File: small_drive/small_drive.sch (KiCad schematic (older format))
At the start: 79 parts, among them CON1 BARREL_JACK, J1 DB9, M1 SiR826DP, M2 SiR826DP, M3 SiR826DP, M4 SiR826DP, M5 SiR826DP, M6 SiR826DP, P2 CONN_01X04, P3 CONN_01X06, P4 CONN_01X08, P5 CONN_01X02, P6 CONN_01X02, P7 CONN_01X02, U1 STM32F334K8, U10 LM5106, U11 ACS711ELCTR-25AB-T, U12 ACS711ELCTR-25AB-T, U13 ACS711ELCTR-25AB-T, U2 OKR_T3, U3 LTC2850, U4 LTC2850, U5 LTC2850, U6 LT1764EQ, U7 MC33074DTBR2, U8 LM5106, U9 LM5106

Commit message: Before splitting.
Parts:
- added C? (x2): C, symbol C
- added Y?: Crystal, symbol Crystal
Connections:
- wire segments 350 -> 360
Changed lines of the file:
@@
 Wire Wire Line
 	2750 4300 2750 4400
+$Comp
+L Crystal Y?
+U 1 1 578406AE
+P 2000 4600
+F 0 "Y?" H 2000 4750 50  0000 C CNN
+F 1 "Crystal" H 2000 4450 50  0000 C CNN
+F 2 "" H 2000 4600 50  0000 C CNN
+F 3 "" H 2000 4600 50  0000 C CNN
+	1    2000 4600
+	1    0    0    -1
+$EndComp
+$Comp
+L C C?
+U 1 1 578407A7
+P 1750 4200
+F 0 "C?" H 1800 4300 50  0000 L CNN
+F 1 "C" H 1800 4100 50  0000 L CNN
+F 2 "" H 1750 4200 60  0000 C CNN
+F 3 "" H 1750 4200 60  0000 C CNN
+	1    1750 4200
+	1    0    0    -1
+$EndComp
+$Comp
+L C C?
+U 1 1 5784091C
+P 2250 4200
+F 0 "C?" H 2300 4300 50  0000 L CNN
+F 1 "C" H 2300 4100 50  0000 L CNN
+F 2 "" H 2250 4200 60  0000 C CNN
+F 3 "" H 2250 4200 60  0000 C CNN
+	1    2250 4200
+	1    0    0    -1
+$EndComp
+Wire Wire Line
+	2250 4400 2250 4950
+Wire Wire Line
+	2250 4600 2150 4600
+Wire Wire Line
+	2250 4950 1450 4950
+Connection ~ 2250 4600
+Wire Wire Line
+	1450 4850 1750 4850
+Wire Wire Line
+	1750 4850 1750 4400
+Wire Wire Line
+	1750 4600 1850 4600
+Connection ~ 1750 4600
+$Comp
+L GND #PWR?
+U 1 1 57841258
+P 2000 3900
+F 0 "#PWR?" H 2000 3650 50  0001 C CNN
+F 1 "GND" H 2000 3750 50  0000 C CNN
+F 2 "" H 2000 3900 50  0000 C CNN
+F 3 "" H 2000 3900 50  0000 C CNN
+	1    2000 3900
+	-1   0    0    1
+$EndComp
+Wire Wire Line
+	2250 3950 2250 4000
+Wire Wire Line
+	1750 3950 2250 3950
+Wire Wire Line
+	1750 3950 1750 4000
+Wire Wire Line
+	2000 3950 2000 3900
+Connection ~ 2000 3950
 $EndSCHEMATC

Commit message: PCB ordered
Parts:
- C48, C49: renamed from C?; footprint (none) -> Capacitors_SMD:C_0603
- Y1: renamed from Y?; footprint (none) -> Crystals:QC3CA

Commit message: Adding order codes
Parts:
- C1, C14, C2, C4, C5, C6: symbol CP -> CP-RESCUE-small_drive
- CON1: Farnell (none) -> 1243245
- P3: Farnell (none) -> 1125375; Manufacturer (none) -> MOLEX; PartNr (none) -> 53261-0671
- P4: Farnell (none) -> 1125376; Manufacturer (none) -> MOLEX; PartNr (none) -> 53261-0871
- U11, U13: value ACS711ELCTR-25AB-T -> ACS711KLCTR-12AB-T; Farnell (none) -> 2057423
- U12: Farnell (none) -> 2057423; PartNr ACS711ELCTR-25AB-T -> ACS711KLCTR-12AB-T
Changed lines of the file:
@@
 $Descr A3 16535 11693
 encoding utf-8
-Sheet 1 4
+Sheet 1 1
 Title ""
 Date ""
@@
 P 14000 3600
 F 0 "U11" H 14000 3900 60  0000 C CNN
-F 1 "ACS711ELCTR-25AB-T" H 14000 3300 60  0000 C CNN
+F 1 "ACS711KLCTR-12AB-T" H 14000 3300 60  0000 C CNN
 F 2 "Housings_SOIC:SOIC-8_3.9x4.9mm_Pitch1.27mm" H 13900 3850 60  0001 C CNN
 F 3 "" H 14000 3600 60  0000 C CNN
-F 4 "620-1371-1-ND" H 14200 4150 60  0001 C CNN "Digikey"
-F 5 "ACS711ELCTR-25AB-T" H 14400 4350 60  0001 C CNN "PartNr"
+F 4 "2057423" H 14000 3600 60  0001 C CNN "Farnell"
+F 5 "620-1371-1-ND" H 14200 4150 60  0001 C CNN "Digikey"
 F 6 "Allegro" H 14300 4250 60  0001 C CNN "Manufacturer"
+F 7 "ACS711ELCTR-25AB-T" H 14400 4350 60  0001 C CNN "PartNr"
 	1    14000 3600
 	1    0    0    -1
@@
 $EndComp
 $Comp
-L GND #PWR02
+L GND-RESCUE-small_drive #PWR02
 U 1 1 5761D72D
 P 10700 2450
@@
 $EndComp
 $Comp
-L GND #PWR04
+L GND-RESCUE-small_drive #PWR04
 U 1 1 5763B708
 P 9800 5050
@@
 F 2 "Housings_SOIC:SOIC-8_3.9x4.9mm_Pitch1.27mm" H 13900 6350 60  0001 C CNN
 F 3 "" H 14000 6100 60  0000 C CNN
-F 4 "620-1371-1-ND" H 14200 6650 60  0001 C CNN "Digikey"
-F 5 "ACS711ELCTR-25AB-T" H 14400 6850 60  0001 C CNN "PartNr"
+F 4 "2057423" H 14000 6100 60  0001 C CNN "Farnell"
+F 5 "620-1371-1-ND" H 14200 6650 60  0001 C CNN "Digikey"
 F 6 "Allegro" H 14300 6750 60  0001 C CNN "Manufacturer"
+F 7 "ACS711KLCTR-12AB-T" H 14400 6850 60  0001 C CNN "PartNr"
 	1    14000 6100
 	1    0    0    -1
@@
 $EndComp
 $Comp
-L GND #PWR07
+L GND-RESCUE-small_drive #PWR07
 U 1 1 576581B1
 P 10700 4950
@@
 $EndComp
 $Comp
-L GND #PWR09
+L GND-RESCUE-small_drive #PWR09
 U 1 1 576581ED
 P 9800 7550
@@
 $EndComp
 $Comp
-L GND #PWR012
+L GND-RESCUE-small_drive #PWR012
 U 1 1 57658859
 P 10700 7450
@@
 $EndComp
 $Comp
-L GND #PWR014
+L GND-RESCUE-small_drive #PWR014
 U 1 1 57658895
 P 9800 10050
@@
 $EndComp
 $Comp
-L GND #PWR016
+L GND-RESCUE-small_drive #PWR016
 U 1 1 57659CCA
 P 12200 4200
@@
 $EndComp
 $Comp
-L GND #PWR017
+L GND-RESCUE-small_drive #PWR017
 U 1 1 57659FBD
 P 12200 6700
@@
 $EndComp
 $Comp
-L GND #PWR018
+L GND-RESCUE-small_drive #PWR018
 U 1 1 5765A1D2
 P 12200 9200
@@
 $EndComp
 $Comp
-L GND #PWR022
+L GND-RESCUE-small_drive #PWR022
 U 1 1 5779740F
 P 4700 9650
@@
 $EndComp
 $Comp
-L GND #PWR023
+L GND-RESCUE-small_drive #PWR023
 U 1 1 577976BF
 P 1550 6750
@@
 $EndComp
 $Comp
-L GND #PWR024
+L GND-RESCUE-small_drive #PWR024
 U 1 1 577978BD
 P 1550 9200
@@
 $EndComp
 $Comp
-L GND #PWR028
+L GND-RESCUE-small_drive #PWR028
 U 1 1 57798BD2
 P 3450 5650
@@
 $EndComp
 $Comp
-L GND #PWR029
+L GND-RESCUE-small_drive #PWR029
 U 1 1 5779A5C8
 P 6950 10000
@@
 $EndComp
 $Comp
-L GND #PWR031
+L GND-RESCUE-small_drive #PWR031
 U 1 1 5779B645
 P 2450 8100
@@
 $EndComp
 $Comp
-L GND #PWR033
+L GND-RESCUE-small_drive #PWR033
 U 1 1 5779C4DD
 P 5700 8600
@@
 $EndComp
 $Comp
-L CP C2
+L CP-RESCUE-small_drive C2
 U 1 1 577CA002
 P 1750 3150
@@
 $EndComp
 $Comp
-L CP C4
+L CP-RESCUE-small_drive C4
 U 1 1 577CA310
 P 2300 3150
@@
 $EndComp
 $Comp
-L CP C5
+L CP-RESCUE-small_drive C5
 U 1 1 577CA388
 P 2850 3150
@@
 $EndComp
 $Comp
-L GND #PWR037
+L GND-RESCUE-small_drive #PWR037
 U 1 1 577CA455
 P 2000 3400
@@
 F 2 "00_Passives:smd_barrel_jack" H 1150 1050 60  0001 C CNN
 F 3 "" H 1150 1050 60  0000 C CNN
+F 4 "1243245" H 1150 1050 60  0001 C CNN "Farnell"
 	1    1150 1050
 	1    0    0    -1
@@
 $EndComp
 $Comp
-L CP C1
+L CP-RESCUE-small_drive C1
 U 1 1 577CE3D8
 P 1700 1250
@@
 $EndComp
 $Comp
-L CP C6
+L CP-RESCUE-small_drive C6
 U 1 1 577CF084
 P 4000 1250
@@
 $EndComp
 $Comp
-L GND #PWR041
+L GND-RESCUE-small_drive #PWR041
 U 1 1 577D3636
 P 4750 2250
@@
 $EndComp
 $Comp
-L CP C14
+L CP-RESCUE-small_drive C14
 U 1 1 577D4059
 P 8350 1250
@@
 F 2 "Connectors_Molex:Molex_PicoBlade_53261-0871" H 7350 9500 50  0001 C CNN
 F 3 "" H 7350 9500 50  0000 C CNN
+F 4 "1125376" H 7350 9500 60  0001 C CNN "Farnell"
+F 5 "MOLEX" H 7350 9500 60  0001 C CNN "Manufacturer"
+F 6 "53261-0871" H 7350 9500 60  0001 C CNN "PartNr"
 	1    7350 9500
 	1    0    0    -1
@@
 F 2 "Connectors_Molex:Molex_PicoBlade_53261-0671" H 6100 8200 50  0001 C CNN
 F 3 "" H 6100 8200 50  0000 C CNN
+F 4 "1125375" H 6100 8200 60  0001 C CNN "Farnell"
+F 5 "MOLEX" H 6100 8200 60  0001 C CNN "Manufacturer"
+F 6 "53261-0671" H 6100 8200 60  0001 C CNN "PartNr"
 	1    6100 8200
 	1    0    0    -1
@@
 P 14000 8600
 F 0 "U13" H 14000 8900 60  0000 C CNN
-F 1 "ACS711ELCTR-25AB-T" H 14000 8300 60  0000 C CNN
+F 1 "ACS711KLCTR-12AB-T" H 14000 8300 60  0000 C CNN
 F 2 "Housings_SOIC:SOIC-8_3.9x4.9mm_Pitch1.27mm" H 13900 8850 60  0001 C CNN
 F 3 "" H 14000 8600 60  0000 C CNN
-F 4 "620-1371-1-ND" H 14200 9150 60  0001 C CNN "Digikey"
-F 5 "ACS711ELCTR-25AB-T" H 14400 9350 60  0001 C CNN "PartNr"
+F 4 "2057423" H 14000 8600 60  0001 C CNN "Farnell"
+F 5 "620-1371-1-ND" H 14200 9150 60  0001 C CNN "Digikey"
 F 6 "Allegro" H 14300 9250 60  0001 C CNN "Manufacturer"
+F 7 "ACS711ELCTR-25AB-T" H 14400 9350 60  0001 C CNN "PartNr"
 	1    14000 8600
 	1    0    0    -1
@@
 $EndComp
 $Comp
-L GND #PWR043
+L GND-RESCUE-small_drive #PWR043
 U 1 1 57818AED
 P 15300 6200
@@
 $EndComp
 $Comp
-L GND #PWR045
+L GND-RESCUE-small_drive #PWR045
 U 1 1 57819A33
 P 15300 8700
@@
 $EndComp
 $Comp
-L GND #PWR047
+L GND-RESCUE-small_drive #PWR047
 U 1 1 57838A84
 P 7650 6150
@@
 	7650 5100 7650 5200
 $Comp
-L GND #PWR049
+L GND-RESCUE-small_drive #PWR049
 U 1 1 5783BEEB
 P 2450 5600
@@
 Connection ~ 2250 4600
 Wire Wire Line
-	1450 4850 1750 4850
-Wire Wire Line
-	1750 4850 1750 4400
+	1750 4850 1450 4850
+Wire Wire Line
+	1750 4400 1750 4850
 Wire Wire Line
 	1750 4600 1850 4600
 Connection ~ 1750 4600
 $Comp
-L GND #PWR051
+L GND-RESCUE-small_drive #PWR051
 U 1 1 57841258
 P 2000 3900

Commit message: Encoder TXD matched with mitsubishi drive.
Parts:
- U10, U8, U9: symbol LM5106-RESCUE-small_drive -> LM5106-RESCUE-small_drive-RESCUE-small_drive
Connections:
- wire segments 360 -> 362
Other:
- moved on the sheet: C14, C15, C16, C17, C18, C8, U6
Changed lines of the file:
@@
 $EndComp
 $Comp
-L LM5106-RESCUE-small_drive U8
+L LM5106-RESCUE-small_drive-RESCUE-small_drive U8
 U 1 1 5761CB0B
 P 11450 3300
@@
 $EndComp
 $Comp
-L LM5106-RESCUE-small_drive U9
+L LM5106-RESCUE-small_drive-RESCUE-small_drive U9
 U 1 1 576581B9
 P 11450 5800
@@
 $EndComp
 $Comp
-L LM5106-RESCUE-small_drive U10
+L LM5106-RESCUE-small_drive-RESCUE-small_drive U10
 U 1 1 57658861
 P 11450 8300
@@
 L LT1764EQ U6
 U 1 1 577CDD60
-P 7500 1100
-F 0 "U6" H 7350 700 60  0000 C CNN
-F 1 "LT1764EQ" H 7500 1400 60  0000 C CNN
-F 2 "00_Passives:DD-PAK" H 7550 1100 60  0001 C CNN
-F 3 "" H 7500 1100 60  0000 C CNN
-F 4 "46" H 7500 1525 60  0001 C CNN "Voorraad"
-	1    7500 1100
+P 7600 1100
+F 0 "U6" H 7450 700 60  0000 C CNN
+F 1 "LT1764EQ" H 7600 1400 60  0000 C CNN
+F 2 "00_Passives:DD-PAK" H 7650 1100 60  0001 C CNN
+F 3 "" H 7600 1100 60  0000 C CNN
+F 4 "46" H 7600 1525 60  0001 C CNN "Voorraad"
+	1    7600 1100
 	1    0    0    -1
 $EndComp
@@
 L C C15
 U 1 1 577D4053
-P 8900 1250
-F 0 "C15" H 8950 1350 50  0000 L CNN
-F 1 "100nF" H 8950 1150 50  0000 L CNN
-F 2 "Capacitors_SMD:C_0603" H 8900 1250 60  0001 C CNN
-F 3 "" H 8900 1250 60  0000 C CNN
-	1    8900 1250
+P 9000 1250
+F 0 "C15" H 9050 1350 50  0000 L CNN
+F 1 "100nF" H 9050 1150 50  0000 L CNN
+F 2 "Capacitors_SMD:C_0603" H 9000 1250 60  0001 C CNN
+F 3 "" H 9000 1250 60  0000 C CNN
+	1    9000 1250
 	1    0    0    -1
 $EndComp
@@
 L CP-RESCUE-small_drive C14
 U 1 1 577D4059
-P 8350 1250
-F 0 "C14" H 8375 1350 50  0000 L CNN
-F 1 "100uF/35V" H 8375 1150 50  0000 L CNN
-F 2 "Capacitors_SMD:c_elec_8x10.5" H 8388 1100 50  0001 C CNN
-F 3 "" H 8350 1250 50  0000 C CNN
-	1    8350 1250
+P 8450 1250
+F 0 "C14" H 8475 1350 50  0000 L CNN
+F 1 "100uF/35V" H 8475 1150 50  0000 L CNN
+F 2 "Capacitors_SMD:c_elec_8x10.5" H 8488 1100 50  0001 C CNN
+F 3 "" H 8450 1250 50  0000 C CNN
+	1    8450 1250
 	1    0    0    -1
 $EndComp
@@
 L C C16
 U 1 1 577D405F
-P 9250 1250
-F 0 "C16" H 9300 1350 50  0000 L CNN
-F 1 "100nF" H 9300 1150 50  0000 L CNN
-F 2 "Capacitors_SMD:C_0603" H 9250 1250 60  0001 C CNN
-F 3 "" H 9250 1250 60  0000 C CNN
-	1    9250 1250
+P 9350 1250
+F 0 "C16" H 9400 1350 50  0000 L CNN
+F 1 "100nF" H 9400 1150 50  0000 L CNN
+F 2 "Capacitors_SMD:C_0603" H 9350 1250 60  0001 C CNN
+F 3 "" H 9350 1250 60  0000 C CNN
+	1    9350 1250
 	1    0    0    -1
 $EndComp
@@
 L C C17
 U 1 1 577D4065
-P 9600 1250
-F 0 "C17" H 9650 1350 50  0000 L CNN
-F 1 "100nF" H 9650 1150 50  0000 L CNN
-F 2 "Capacitors_SMD:C_0603" H 9600 1250 60  0001 C CNN
-F 3 "" H 9600 1250 60  0000 C CNN
-	1    9600 1250
+P 9700 1250
+F 0 "C17" H 9750 1350 50  0000 L CNN
+F 1 "100nF" H 9750 1150 50  0000 L CNN
+F 2 "Capacitors_SMD:C_0603" H 9700 1250 60  0001 C CNN
+F 3 "" H 9700 1250 60  0000 C CNN
+	1    9700 1250
 	1    0    0    -1
 $EndComp
@@
 L C C18
 U 1 1 577D406B
-P 9950 1250
-F 0 "C18" H 10000 1350 50  0000 L CNN
-F 1 "100nF" H 10000 1150 50  0000 L CNN
-F 2 "Capacitors_SMD:C_0603" H 9950 1250 60  0001 C CNN
-F 3 "" H 9950 1250 60  0000 C CNN
-	1    9950 1250
+P 10050 1250
+F 0 "C18" H 10100 1350 50  0000 L CNN
+F 1 "100nF" H 10100 1150 50  0000 L CNN
+F 2 "Capacitors_SMD:C_0603" H 10050 1250 60  0001 C CNN
+F 3 "" H 10050 1250 60  0000 C CNN
+	1    10050 1250
 	1    0    0    -1
 $EndComp
@@
 L +3.3V #PWR042
 U 1 1 577D4C40
-P 8600 750
-F 0 "#PWR042" H 8650 780 20  0001 C CNN
-F 1 "+3.3V" H 8600 840 30  0000 C CNN
-F 2 "" H 8600 750 60  0000 C CNN
-F 3 "" H 8600 750 60  0000 C CNN
-	1    8600 750
+P 8700 750
+F 0 "#PWR042" H 8750 780 20  0001 C CNN
+F 1 "+3.3V" H 8700 840 30  0000 C CNN
+F 2 "" H 8700 750 60  0000 C CNN
+F 3 "" H 8700 750 60  0000 C CNN
+	1    8700 750
 	1    0    0    -1
 $EndComp
@@
 L C C8
 U 1 1 57814D4F
-P 10300 1250
-F 0 "C8" H 10350 1350 50  0000 L CNN
-F 1 "100nF" H 10350 1150 50  0000 L CNN
-F 2 "Capacitors_SMD:C_0603" H 10300 1250 60  0001 C CNN
-F 3 "" H 10300 1250 60  0000 C CNN
-	1    10300 1250
+P 10400 1250
+F 0 "C8" H 10450 1350 50  0000 L CNN
+F 1 "100nF" H 10450 1150 50  0000 L CNN
+F 2 "Capacitors_SMD:C_0603" H 10400 1250 60  0001 C CNN
+F 3 "" H 10400 1250 60  0000 C CNN
+	1    10400 1250
 	1    0    0    -1
 $EndComp
@@
 	1500 1050 1500 2200
 Wire Wire Line
-	1500 2200 10300 2200
-Wire Wire Line
-	7500 2200 7500 1750
-Wire Wire Line
-	3850 950  6950 950
+	1500 2200 10400 2200
+Wire Wire Line
+	7600 2200 7600 1750
+Wire Wire Line
+	3850 950  7050 950
 Wire Wire Line
 	6650 950  6650 1050
@@
 Connection ~ 4750 2200
 Wire Wire Line
-	8350 950  8350 1100
-Wire Wire Line
-	8350 1400 8350 2200
-Wire Wire Line
-	8900 2200 8900 1450
-Wire Wire Line
-	9250 1450 9250 2200
-Wire Wire Line
-	9600 2200 9600 1450
-Wire Wire Line
-	9950 2200 9950 1450
-Wire Wire Line
-	8050 950  10300 950
-Wire Wire Line
-	9950 950  9950 1050
-Wire Wire Line
-	9600 1050 9600 950
-Connection ~ 9600 950
-Wire Wire Line
-	9250 950  9250 1050
-Connection ~ 9250 950
-Wire Wire Line
-	8900 1050 8900 950
-Connection ~ 8900 950
-Connection ~ 7500 2200
-Connection ~ 8350 2200
-Connection ~ 8900 2200
-Connection ~ 9250 2200
-Connection ~ 9600 2200
-Connection ~ 8350 950
-Wire Wire Line
-	8600 750  8600 950
-Connection ~ 8600 950
+	8450 950  8450 1100
+Wire Wire Line
+	8450 1400 8450 2200
+Wire Wire Line
+	9000 2200 9000 1450
+Wire Wire Line
+	9350 1450 9350 2200
+Wire Wire Line
+	9700 2200 9700 1450
+Wire Wire Line
+	10050 2200 10050 1450
+Wire Wire Line
+	8150 950  10400 950
+Wire Wire Line
+	10050 950  10050 1050
+Wire Wire Line
+	9700 1050 9700 950
+Connection ~ 9700 950
+Wire Wire Line
+	9350 950  9350 1050
+Connection ~ 9350 950
+Wire Wire Line
+	9000 1050 9000 950
+Connection ~ 9000 950
+Connection ~ 7600 2200
+Connection ~ 8450 2200
+Connection ~ 9000 2200
+Connection ~ 9350 2200
+Connection ~ 9700 2200
+Connection ~ 8450 950
+Wire Wire Line
+	8700 750  8700 950
+Connection ~ 8700 950
 Wire Wire Line
 	3000 5050 3550 5050
@@
 	3000 5150 3550 5150
 Wire Wire Line
-	8100 950  8100 1200
-Wire Wire Line
-	8100 1200 8050 1200
-Connection ~ 8100 950
+	8200 950  8200 1200
+Wire Wire Line
+	8200 1200 8150 1200
+Connection ~ 8200 950
 Wire Wire Line
 	2500 950  2500 1200
@@
 	1450 7600 2250 7600
 Wire Wire Line
-	10300 950  10300 1050
-Connection ~ 9950 950
-Wire Wire Line
-	10300 2200 10300 1450
-Connection ~ 9950 2200
+	10400 950  10400 1050
+Connection ~ 10050 950
+Wire Wire Line
+	10400 2200 10400 1450
+Connection ~ 10050 2200
 Wire Wire Line
 	5800 7900 5800 8450
@@
 	2000 3950 2000 3900
 Connection ~ 2000 3950
+Wire Wire Line
+	7000 950  7000 1200
+Wire Wire Line
+	7000 1200 7050 1200
+Connection ~ 7000 950
 $EndSCHEMATC

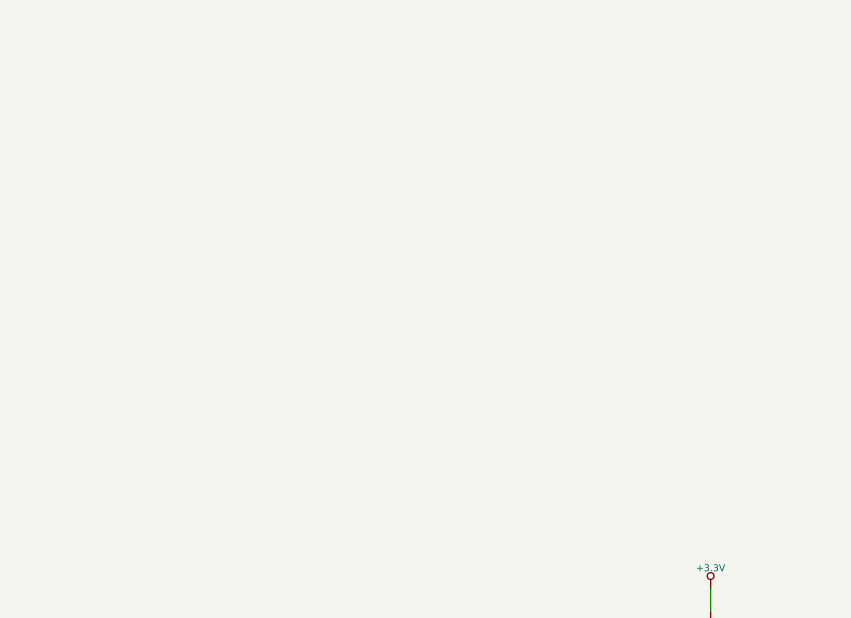
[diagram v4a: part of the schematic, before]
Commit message: Oops wrong sign for phase->orth current.
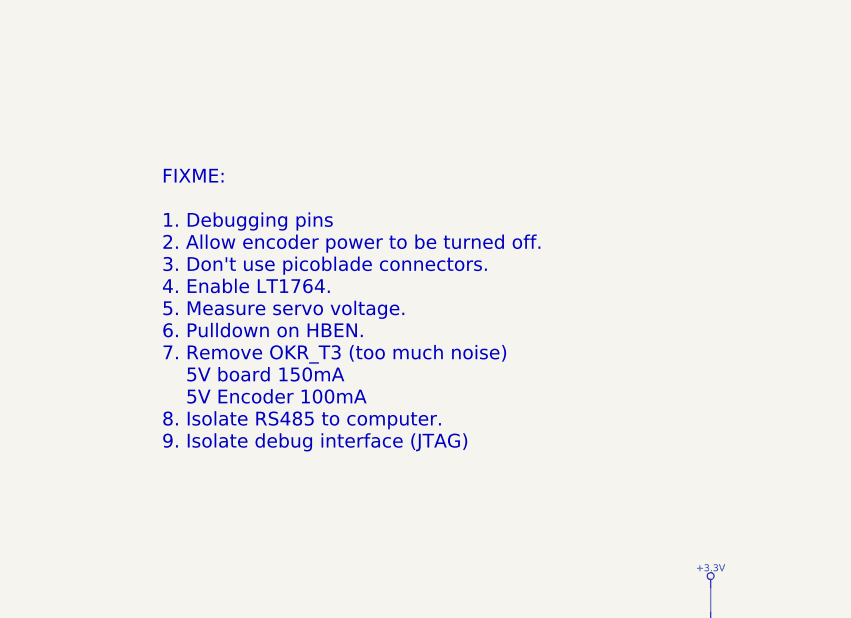
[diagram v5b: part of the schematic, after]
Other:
- note added: "FIXME:\n\n1. Debugging pins\n2. Allow encoder power to be turned off.\n3. Don't use picoblade connectors.\n4. Enable LT1764.\n5. Measure servo voltage.\n6. Pulldown on HBEN.\n7. Remove OKR_T3 (too much noise) \n 5V board 150mA\n 5V Encoder 100mA\n8. Isolate RS485 to computer.\n9. Isolate debug interface (JTAG)"
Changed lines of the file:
@@
 	7000 1200 7050 1200
 Connection ~ 7000 950
+Text Notes 5250 4500 0    60   ~ 0
+FIXME:\n\n1. Debugging pins\n2. Allow encoder power to be turned off.\n3. Don't use picoblade connectors.\n4. Enable LT1764.\n5. Measure servo voltage.\n6. Pulldown on HBEN.\n7. Remove OKR_T3 (too much noise) \n    5V board 150mA\n    5V Encoder 100mA\n8. Isolate RS485 to computer.\n9. Isolate debug interface (JTAG)
 $EndSCHEMATC

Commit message: Pauze klus.
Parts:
- removed CON1: BARREL_JACK, 00_Passives:smd_barrel_jack, symbol BARREL_JACK
- removed P3: CONN_01X06, Connectors_Molex:Molex_PicoBlade_53261-0671, symbol CONN_01X06
- removed P4: CONN_01X08, Connectors_Molex:Molex_PicoBlade_53261-0871, symbol CONN_01X08
- removed U1: STM32F334K8, Housings_QFP:LQFP-32_7x7mm_Pitch0.8mm, symbol STM32F334K8
- removed U2: OKR_T3, 00_Passives:okr_t3, symbol OKR_T3
- removed U3, U5: LTC2850, Housings_SOIC:SOIC-8_3.9x4.9mm_Pitch1.27mm, symbol LTC2850-RESCUE-small_drive
- added C10, C11, C28, C29, C33, C37, C39, C40, C41, C42, C43, C45, C50, C51, C52, C53, C54, C55, C56, C57, C58, C59: 100nF, Capacitors_SMD:C_0603, symbol C
- added C30, C31: 10uF, Capacitors_SMD:C_1210, symbol C
- added C32, C34, C36, C38: 100uF/35V, Capacitors_SMD:c_elec_8x10.5, symbol CP-RESCUE-small_drive
- added C35: 10nF, Capacitors_SMD:C_0603, symbol C
- added C44: 2.2uF, Capacitors_SMD:C_1206, symbol C
- added C46: 25pF, Capacitors_SMD:C_0603, symbol C
- added J2: DB15, Connectors_Amphenol:DB15F_HD20_SIZE2, symbol DB15
- added P1: CONN_01X04, Connect:bornier4, symbol CONN_01X04
- added P3: CONN_01X04, Pin_Headers:Pin_Header_Straight_1x04, symbol CONN_01X04
- added R18, R27, R28: 510, Resistors_SMD:R_0603, symbol R
- added R19, R20, R25, R26: 1k, Resistors_SMD:R_0603, symbol R
- added R21, R22, R23, R24, R38, R39, R40, R41, R42, R43, R46: R, Resistors_SMD:R_0603, symbol R
- added R29, R30, R31: 680, Resistors_SMD:R_0603, symbol R
- added R33: 300, Resistors_SMD:R_0603, symbol R
- added R34: 56k, Resistors_SMD:R_0603, symbol R
- added R35: 6.49k, Resistors_SMD:R_0603, symbol R
- added R36, R37: 220, Resistors_SMD:R_0603, symbol R
- added R44, R45: 22, Resistors_SMD:R_0603, symbol R
- added U1: XMC4400-F64x512, Housings_QFP:LQFP-64-1EP_10x10mm_Pitch0.5mm, symbol XMC4400-F64x512
- added U14, U5: AD8226, Housings_SOIC:SOIC-8_3.9x4.9mm_Pitch1.27mm, symbol AD8226
- added U15: MAX3096, Housings_SOIC:SOIC-16_3.9x9.9mm_Pitch1.27mm, symbol MAX3096
- added U16: AMC1203, 00_Passives:SO8_11, symbol AMC1203
- added U17: 7805, 00_Local:TO220_78xx, symbol 7805
- added U18: LT1764EQ, 00_Passives:DD-PAK, symbol LT1764EQ
- added U19: KSZ8081, Housings_DFN_QFN:QFN-24-1EP_4x4mm_Pitch0.5mm, symbol KSZ8081
- added U2, U3: ips511g, Housings_SOIC:SOIC-8_3.9x4.9mm_Pitch1.27mm, symbol ips511g
- added U20: ETH100_MAG, 00_Passives:ETH100_MAG, symbol ETH100_MAG
- added X1, X2: NKE1212DC, 00_Local:NKE-SC, symbol NKE1212DC
- added X3, X4, X5, X6: HCPL0201, Housings_SOIC:SOIC-8_3.9x4.9mm_Pitch1.27mm, symbol HCPL0201
- added Y2: 25MHz, Crystals:crystal_FA238-TSX3225, symbol Crystal
- C47: value 100nF -> 25pF
- C48, C49: value C -> 15pF
- J1: footprint Connect:DB9FC -> Connectors_Amphenol:DB9FC_HD-20; Farnell (none) -> 1653978; Manufacturer (none) -> AMP; PartNr (none) -> 1734354-1
- M1, M2, M3, M4, M5, M6: footprint 00_Passives:SOT-669_GDS -> 00_Passives:SOT-669_GDS_therma
- R1: value 270 -> 10k
- R15, R16, R17: value R -> 10k
- R32: value 0 -> 680
- Y1: value Crystal -> 12MHz
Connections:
- net labels added: +12P, +3.3VADC, +5P, -12V, ENC_12V, ENC_5V, ENC_A, ENC_B, ENC_COS, ENC_DIR, ENC_RXD2, ENC_SIN, ENC_Z, ETH0_CLK_RMIIA, ETH0_MDC, ETH0_MDIO, ETH0_RXD0A, ETH0_RXD1A, ETH0_RXERA, ETH0_TXD0, ETH0_TXD1, ETH0_TX_EN, ETH0_~RST, ETH_CRS_DVA, GNDPWR, LED4, MCLK, MDAT, VddC
- net labels removed: DXD, RXD, SWCLK, SWDAT, TXD
- wire segments 362 -> 650
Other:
- note added: "FIXME:\n\n1. Debugging pins\n2. 1.65V ref voor sincos.\n3. pinning xmc4500 checken."
- note added: "Using POSIF_0B and ADC_G[01]CH6"
- note removed: "FIXME:\n\n1. Debugging pins\n2. Allow encoder power to be turned off.\n3. Don't use picoblade connectors.\n4. Enable LT1764.\n5. Measure servo voltage.\n6. Pulldown on HBEN.\n7. Remove OKR_T3 (too much noise) \n 5V board 150mA\n 5V Encoder 100mA\n8. Isolate RS485 to computer.\n9. Isolate debug interface (JTAG)"
- note removed: "Just for routing"
- moved on the sheet: C1, C12, C13, C14, C15, C16, C17, C18, C19, C2, C20, C21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
